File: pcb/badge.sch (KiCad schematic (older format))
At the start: 26 parts, among them IC102 AAT3681A, P1 CONN_01X04, P102 CONN_01X02, P103 USB_OTG, P2 CONNECTOR, P3 CONNECTOR, Q1 NPN, Q101 FT230XS-R, Q102 NPN

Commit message: started schema
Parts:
- removed D1, D2, D3: LED, netl:SMD_0603, symbol LED
- removed IC102: AAT3681A, netl:SC70JW-8, symbol AAT3681A
- removed P2, P3: CONNECTOR, netl:1Pin_small, symbol CONNECTOR
- removed Q101: FT230XS-R, Housings_SSOP:SSOP-16_5.3x6.2mm_Pitch0.65mm, symbol FT230XS-R
- removed R105, R3, R4, R5: R, netl:SMD_0603, symbol R
- added C? (x2): C, symbol C
- added IC?: TP4056, symbol TP4056
- added IC?: CH340G, symbol CH340G
- added R?: R, symbol R
- added X?: CRYSTAL_SMD, symbol CRYSTAL_SMD
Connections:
- net labels added: RX, TX
- net labels removed: chrg
- wire segments 72 -> 64
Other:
- moved on the sheet: C1, C104, Q1, Q102, R1, R107, R108, R2

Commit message: first complete version
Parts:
- removed R6: 0R, netl:SMD_0603, symbol R
- removed X?: CRYSTAL_SMD, symbol CRYSTAL_SMD
- added D101: LED, netl:SMD_0603, symbol LED
- added R101: R, netl:SMD_0603, symbol R
- added x101: xtal_osc, netl:SM_3225, symbol xtal_osc
- C103, C104: renamed from C?; footprint (none) -> netl:SMD_0603
- IC101: renamed from IC?; footprint (none) -> Housings_SOIC:SOIC-16_3.9x9.9mm_Pitch1.27mm
- IC102: renamed from IC?; footprint (none) -> SMD_Packages:SOIC-8-N
- P103: renamed from P1; value CONN_01X04 -> CONN_01X05; footprint Pin_Headers:Pin_Header_Angled_1x04 -> Pin_Headers:Pin_Header_Angled_1x05; symbol CONN_01X04 -> CONN_01X05
- R104: renamed from R?; footprint (none) -> netl:SMD_0603
- renumbered 0R1 to 0R101, 0R2 to 0R102, 0R3 to 0R103, C104 to C101, C1 to C102, P102 to P101, P103 to P102, Q1 to Q101, R1 to R102, R2 to R103, R108 to R105, R107 to R106
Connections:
- net AVR_RX: now also P103.3 (P3); no longer P103.2 (P2)
- net AVR_TX: now also P103.2 (P2); no longer P103.1 (P1)
- net AVR_VCC: now also P103.4 (P4); no longer P103.3 (P3)
- net D-: now also P102.2 (D-)
- net GND: now also P103.5 (P5), x101.2, x101.4; no longer P103.4 (P4)
- net VBat: now also P103.1 (P1)
- net V_USB: now also R101.2
- net at IC102.7 (~CHRG): now also D101.1 (K)
- net at C103.1, IC101.7 (XI): now also x101.1
- net at C104.1, IC101.8 (XO): now also x101.3
- new net: D101.2 (A), R101.1
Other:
- note added: "use if no reference from MCU available"
- note removed: "3V3 only for communication, not power\n(plain serial with no li-po)"
- moved on the sheet: C103, C104, IC101

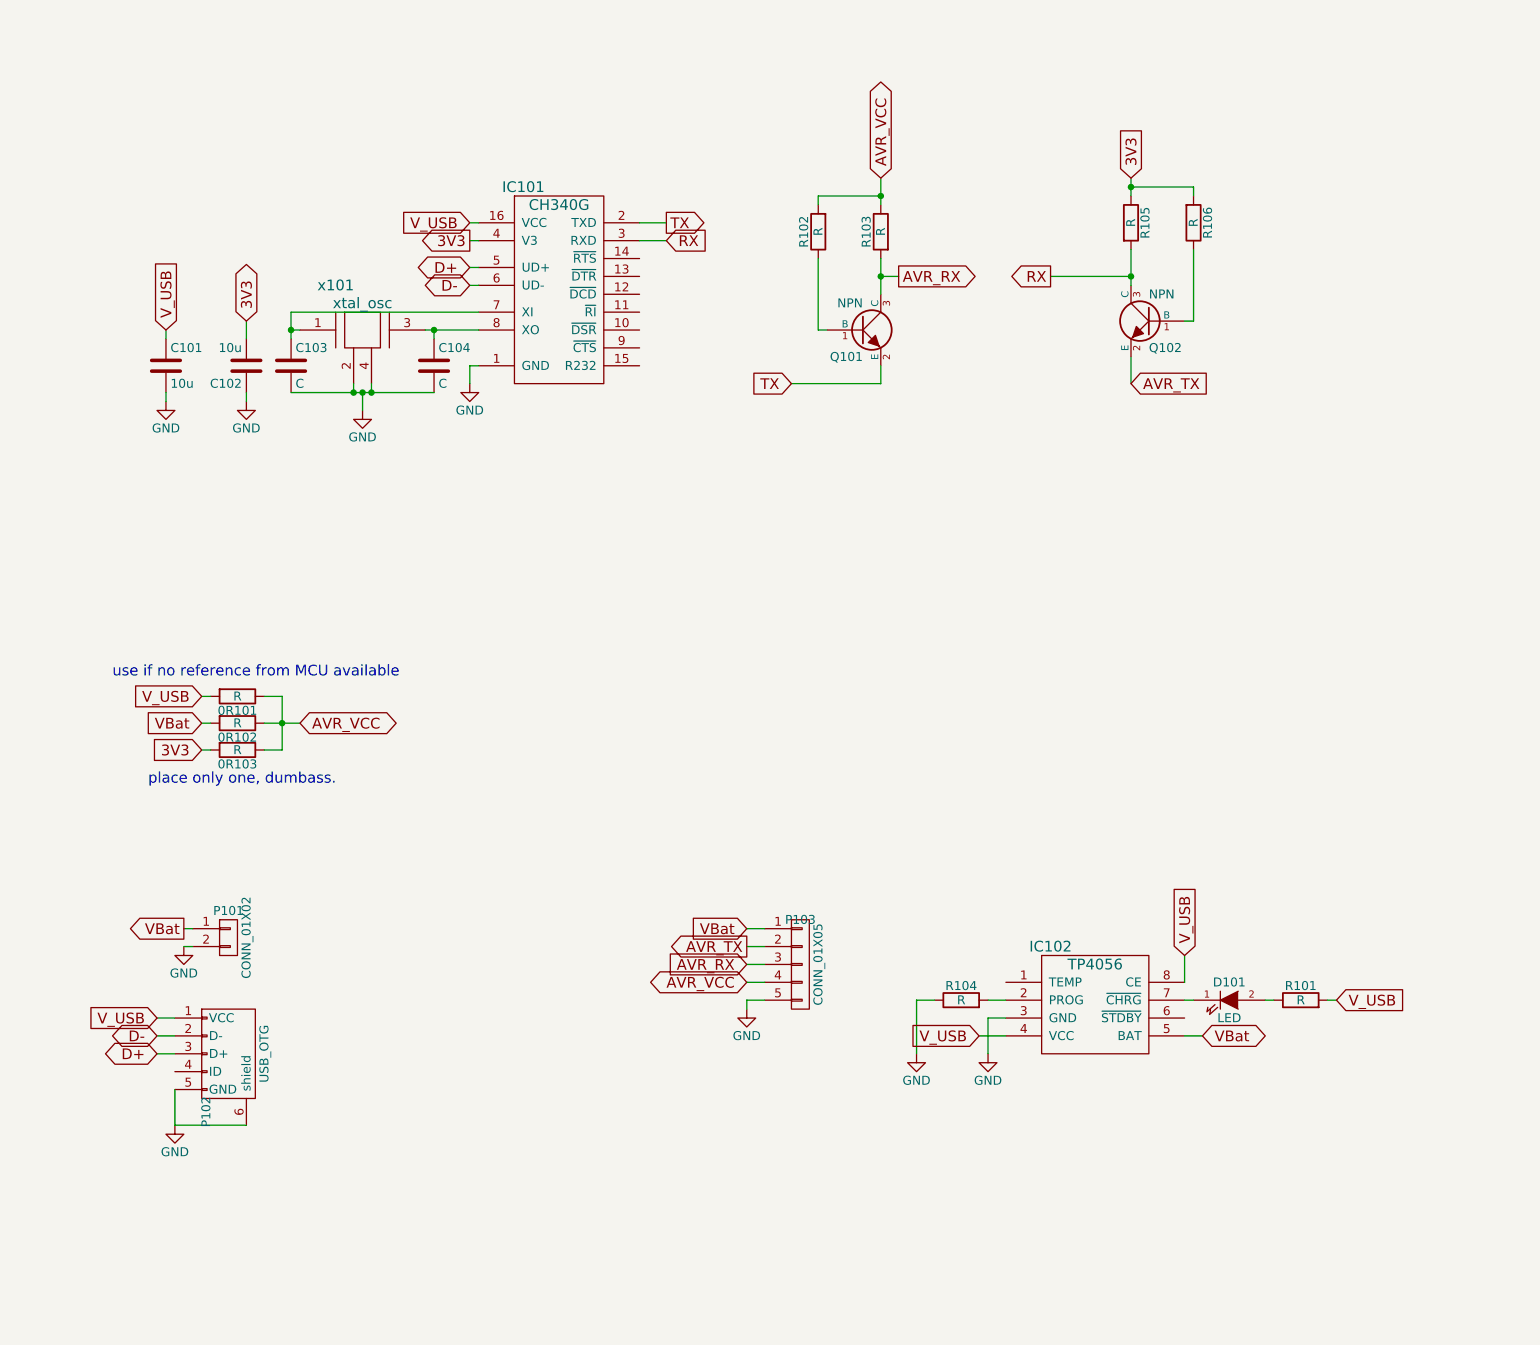
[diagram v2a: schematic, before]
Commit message: remved logic level shifter and updated component values
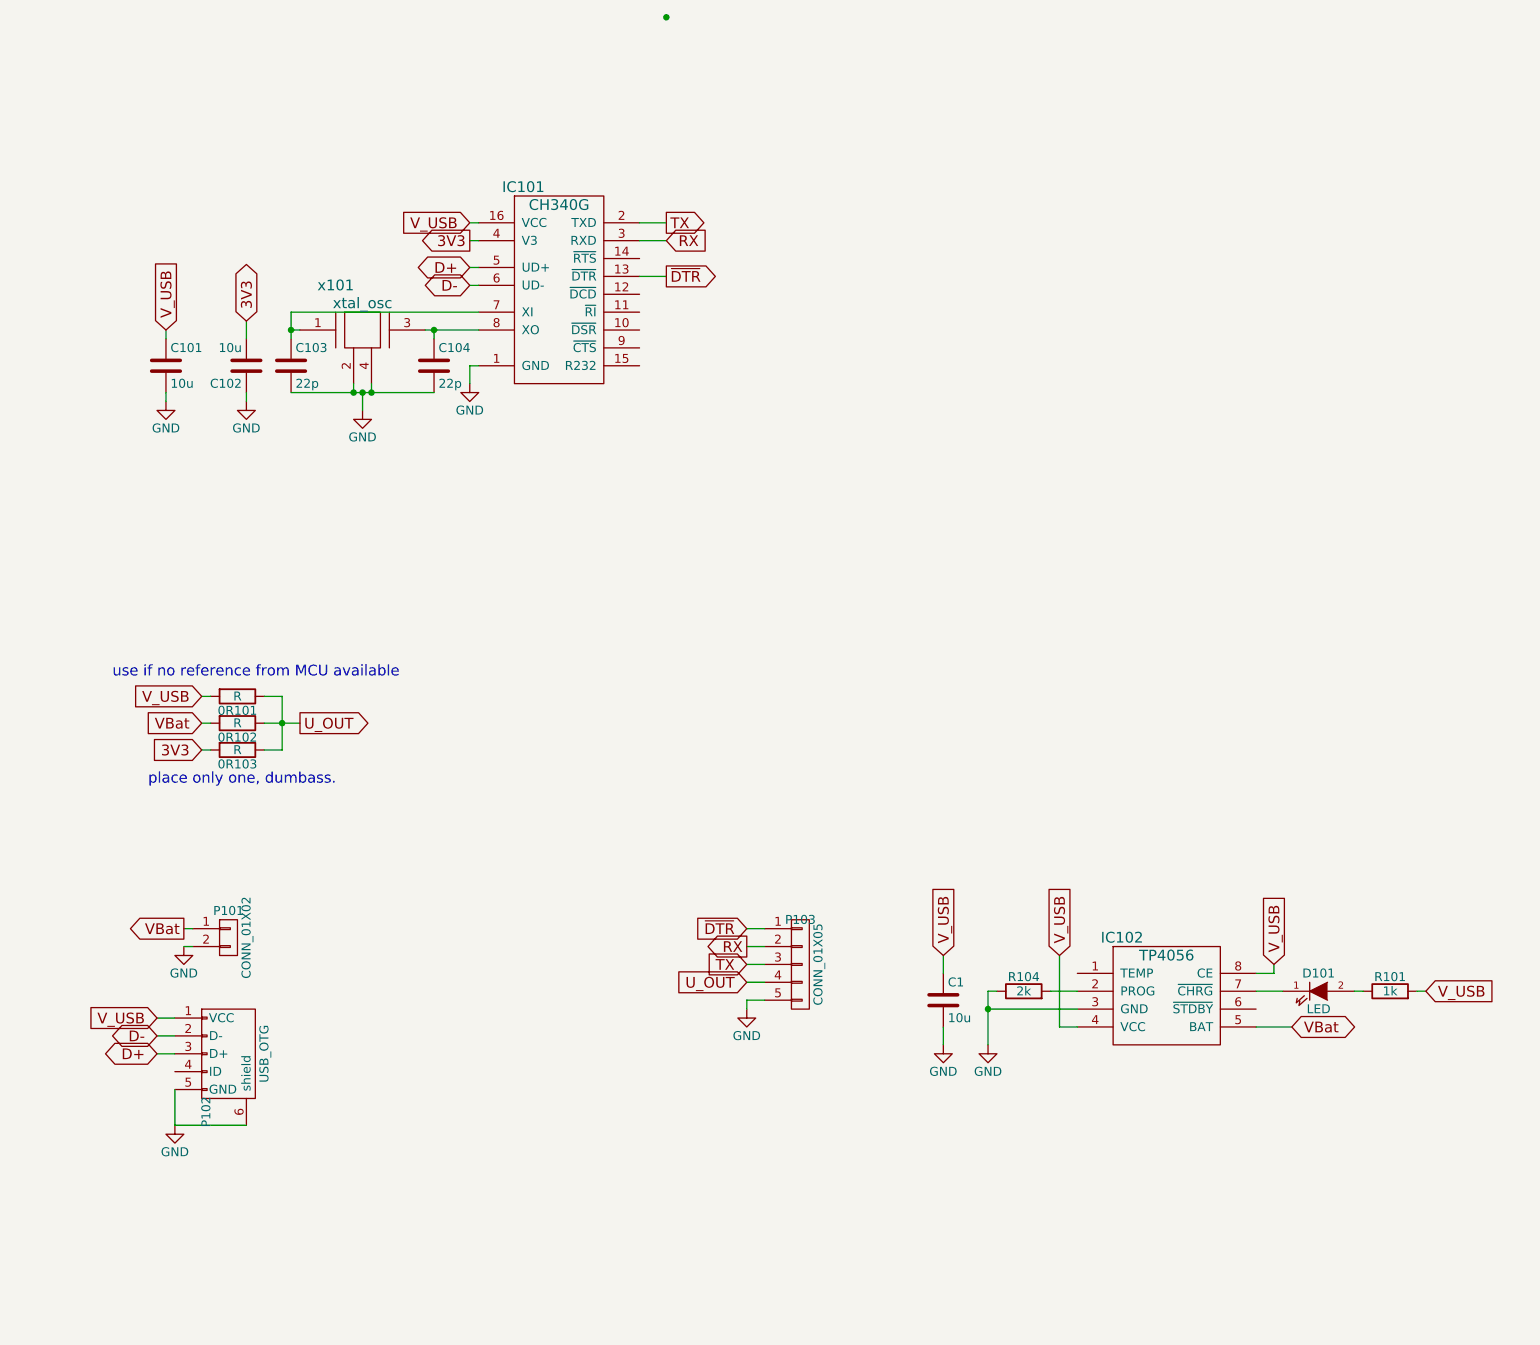
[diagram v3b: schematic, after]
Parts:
- removed Q101, Q102: NPN, TO_SOT_Packages_SMD:SOT-323, symbol NPN
- removed R102, R103, R105, R106: R, netl:SMD_0603, symbol R
- added C1: 10u, netl:SMD_0603, symbol C
- C103, C104: value C -> 22p
- R101: value R -> 1k
- R104: value R -> 2k
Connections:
- net AVR_RX is gone; now on net TX: P103.3 (P3)
- net AVR_TX is gone; now on net RX: P103.2 (P2)
- net GND: now also C1.2
- net VBat: no longer P103.1 (P1)
- net V_USB: now also C1.1
- net ~DTR: now reaches IC101.13 (~DTR)
- net ~DTR: now also P103.1 (P1)
- net AVR_VCC renamed U_OUT
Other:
- moved on the sheet: D101, IC102, R101, R104
